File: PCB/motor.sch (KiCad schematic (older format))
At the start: 28 parts, among them J3 70543-0003, U3 TMC2130-TA

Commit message: Finished TMC2130 placement.
Motor sheets is now instanced. That way I simply could use
a KiCad plugin to duplicate the layout in Pcbnew.
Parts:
- TP11: value X_OA1 -> OA1
- TP12: value X_OA2 -> OA2
- TP13: value X_OB2 -> OB2
- TP14: value X_OB1 -> OB1
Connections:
- net labels added: DIAG, DIR, EN, SS, STEP, VDD_PWR
- net labels removed: SS_X, VDD_IN, X_DIAG, X_DIR, X_EN, X_STEP

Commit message: Finished placement. Currently routing last paths.
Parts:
- removed C14, C24: 100nF, Capacitor_SMD:C_0603_1608Metric, symbol Device:C
- removed C16, C17, C18, C19: 1nF, Capacitor_SMD:C_0603_1608Metric, symbol Device:C
- removed R12, R13, R15, R16: 100, Resistor_SMD:R_0603_1608Metric, symbol Device:R
- C58: renamed from C22; value 4.7uF -> 10uF
- renumbered C13 to C54, C15 to C55, C20 to C56, C21 to C57, C23 to C59, C25 to C60, C26 to C61, C27 to C62, J3 to J21, R14 to R32, R17 to R33, R18 to R34, TP11 to TP27, TP12 to TP28, TP13 to TP29, TP14 to TP30, U3 to U7
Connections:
- wire segments 63 -> 43
- no-connect marks 19 -> 18
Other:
- moved on the sheet: R12, R14

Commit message: Added the secnd Z connection.
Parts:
- renumbered C54 to C13, C55 to C14, C56 to C15, C57 to C16, C58 to C17, C59 to C18, C60 to C19, C61 to C20, C62 to C21, J21 to J3, R32 to R12, R33 to R13, R34 to R14, TP27 to TP11, TP28 to TP12, TP29 to TP13, TP30 to TP14, U7 to U3

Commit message: First PCB version that is fully placed and routed.
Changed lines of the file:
@@
 AR Path="/5AFC9D86/5AF8CE9A" Ref="#PWR0105"  Part="1"
 AR Path="/5AFD185C/5AF8CE9A" Ref="#PWR0118"  Part="1"
-F 0 "#PWR0118" H 3550 3300 50  0001 C CNN
+F 0 "#PWR092" H 3550 3300 50  0001 C CNN
 F 1 "GNDA" H 3555 3377 50  0000 C CNN
 F 2 "" H 3550 3550 50  0001 C CNN
@@
 AR Path="/5AFC9D86/5B0399AA" Ref="#PWR0100"  Part="1"
 AR Path="/5AFD185C/5B0399AA" Ref="#PWR0113"  Part="1"
-F 0 "#PWR0113" H 1750 1900 50  0001 C CNN
+F 0 "#PWR087" H 1750 1900 50  0001 C CNN
 F 1 "GNDA" V 1755 2023 50  0000 R CNN
 F 2 "" H 1750 2150 50  0001 C CNN
@@
 AR Path="/5AFC9D86/5AF8CE9D" Ref="R33"  Part="1"
 AR Path="/5AFD185C/5AF8CE9D" Ref="R36"  Part="1"
-F 0 "R36" H 4820 2796 50  0000 L CNN
+F 0 "R30" H 4820 2796 50  0000 L CNN
 F 1 "10k" H 4820 2705 50  0000 L CNN
 F 2 "Resistor_SMD:R_0603_1608Metric" V 4680 2750 50  0001 C CNN
@@
 AR Path="/5AFC9D86/5AF8CE9F" Ref="#PWR0104"  Part="1"
 AR Path="/5AFD185C/5AF8CE9F" Ref="#PWR0117"  Part="1"
-F 0 "#PWR0117" H 2450 3300 50  0001 C CNN
+F 0 "#PWR091" H 2450 3300 50  0001 C CNN
 F 1 "GNDA" H 2455 3377 50  0000 C CNN
 F 2 "" H 2450 3550 50  0001 C CNN
@@
 AR Path="/5AFC9D86/5AF8CEA1" Ref="C55"  Part="1"
 AR Path="/5AFD185C/5AF8CEA1" Ref="C64"  Part="1"
-F 0 "C64" H 3565 1646 50  0000 L CNN
+F 0 "C46" H 3565 1646 50  0000 L CNN
 F 1 "100nF" H 3565 1555 50  0000 L CNN
 F 2 "Capacitor_SMD:C_0603_1608Metric" H 3488 1450 50  0001 C CNN
@@
 AR Path="/5AFC9D86/5AF8CEA3" Ref="C56"  Part="1"
 AR Path="/5AFD185C/5AF8CEA3" Ref="C65"  Part="1"
-F 0 "C65" V 3698 1700 50  0000 C CNN
+F 0 "C47" V 3698 1700 50  0000 C CNN
 F 1 "22nF" V 3789 1700 50  0000 C CNN
 F 2 "Capacitor_SMD:C_0603_1608Metric" H 3988 1550 50  0001 C CNN
@@
 AR Path="/5AFC9D86/5B03C54C" Ref="C54"  Part="1"
 AR Path="/5AFD185C/5B03C54C" Ref="C63"  Part="1"
-F 0 "C63" H 3765 1146 50  0000 L CNN
+F 0 "C45" H 3765 1146 50  0000 L CNN
 F 1 "100nF" H 3765 1055 50  0000 L CNN
 F 2 "Capacitor_SMD:C_0603_1608Metric" H 3688 950 50  0001 C CNN
@@
 AR Path="/5AFC9D86/5B03CBB9" Ref="#PWR096"  Part="1"
 AR Path="/5AFD185C/5B03CBB9" Ref="#PWR0109"  Part="1"
-F 0 "#PWR0109" H 3650 1000 50  0001 C CNN
+F 0 "#PWR083" H 3650 1000 50  0001 C CNN
 F 1 "GNDA" H 3655 1077 50  0000 C CNN
 F 2 "" H 3650 1250 50  0001 C CNN
@@
 AR Path="/5AFC9D86/5B03D7F6" Ref="C57"  Part="1"
 AR Path="/5AFD185C/5B03D7F6" Ref="C66"  Part="1"
-F 0 "C66" H 4385 2054 50  0000 R CNN
+F 0 "C48" H 4385 2054 50  0000 R CNN
 F 1 "470nF" H 4385 2145 50  0000 R CNN
 F 2 "Capacitor_SMD:C_0603_1608Metric" H 4538 1950 50  0001 C CNN
@@
 AR Path="/5AFC9D86/5AF8CEA9" Ref="#PWR098"  Part="1"
 AR Path="/5AFD185C/5AF8CEA9" Ref="#PWR0111"  Part="1"
-F 0 "#PWR0111" H 4500 1700 50  0001 C CNN
+F 0 "#PWR085" H 4500 1700 50  0001 C CNN
 F 1 "GNDA" H 4505 1777 50  0000 C CNN
 F 2 "" H 4500 1950 50  0001 C CNN
@@
 AR Path="/5AFC9D86/5AF8CEAA" Ref="C59"  Part="1"
 AR Path="/5AFD185C/5AF8CEAA" Ref="C68"  Part="1"
-F 0 "C68" H 1365 3146 50  0000 L CNN
+F 0 "C50" H 1365 3146 50  0000 L CNN
 F 1 "100nF" H 1365 3055 50  0000 L CNN
 F 2 "Capacitor_SMD:C_0603_1608Metric" H 1288 2950 50  0001 C CNN
@@
 AR Path="/5AFC9D86/5B03E652" Ref="#PWR0103"  Part="1"
 AR Path="/5AFD185C/5B03E652" Ref="#PWR0116"  Part="1"
-F 0 "#PWR0116" H 1250 3000 50  0001 C CNN
+F 0 "#PWR090" H 1250 3000 50  0001 C CNN
 F 1 "GNDA" H 1255 3077 50  0000 C CNN
 F 2 "" H 1250 3250 50  0001 C CNN
@@
 AR Path="/5AFC9D86/5B043BF7" Ref="#PWR0102"  Part="1"
 AR Path="/5AFD185C/5B043BF7" Ref="#PWR0115"  Part="1"
-F 0 "#PWR0115" H 4150 2200 50  0001 C CNN
+F 0 "#PWR089" H 4150 2200 50  0001 C CNN
 F 1 "GNDA" V 4155 2322 50  0000 R CNN
 F 2 "" H 4150 2450 50  0001 C CNN
@@
 AR Path="/5AFC9D86/5AF8CEAE" Ref="C58"  Part="1"
 AR Path="/5AFD185C/5AF8CEAE" Ref="C67"  Part="1"
-F 0 "C67" V 5600 2350 50  0000 R CNN
+F 0 "C49" V 5600 2350 50  0000 R CNN
 F 1 "10uF" V 5700 2450 50  0000 R CNN
 F 2 "Capacitor_SMD:C_0603_1608Metric" H 5488 2200 50  0001 C CNN
@@
 AR Path="/5AFC9D86/5AF8CEAF" Ref="#PWR0101"  Part="1"
 AR Path="/5AFD185C/5AF8CEAF" Ref="#PWR0114"  Part="1"
-F 0 "#PWR0114" H 5600 2100 50  0001 C CNN
+F 0 "#PWR088" H 5600 2100 50  0001 C CNN
 F 1 "GNDA" H 5605 2177 50  0000 C CNN
 F 2 "" H 5600 2350 50  0001 C CNN
@@
 AR Path="/5AFC9D86/5AF8CEB0" Ref="R34"  Part="1"
 AR Path="/5AFD185C/5AF8CEB0" Ref="R37"  Part="1"
-F 0 "R37" H 3100 4050 50  0000 R CNN
+F 0 "R31" H 3100 4050 50  0000 R CNN
 F 1 "0.12" H 3100 4150 50  0000 R CNN
 F 2 "Resistor_SMD:R_1206_3216Metric" V 2780 4100 50  0001 C CNN
@@
 AR Path="/5AFC9D86/5AF8CEB4" Ref="#PWR0106"  Part="1"
 AR Path="/5AFD185C/5AF8CEB4" Ref="#PWR0119"  Part="1"
-F 0 "#PWR0119" H 2850 4000 50  0001 C CNN
+F 0 "#PWR093" H 2850 4000 50  0001 C CNN
 F 1 "GNDA" H 2855 4077 50  0000 C CNN
 F 2 "" H 2850 4250 50  0001 C CNN
@@
 AR Path="/5AFC9D86/5B09FBAD" Ref="J22"  Part="1"
 AR Path="/5AFD185C/5B09FBAD" Ref="J23"  Part="1"
-F 0 "J23" H 7529 1292 50  0000 L CNN
+F 0 "J21" H 7529 1292 50  0000 L CNN
 F 1 "70543-0003" H 7529 1201 50  0000 L CNN
 F 2 "custom-footprints:70543-0003" H 7450 1300 50  0001 C CNN
@@
 AR Path="/5AFC9D86/5B09FBB4" Ref="TP28"  Part="1"
 AR Path="/5AFD185C/5B09FBB4" Ref="TP32"  Part="1"
-F 0 "TP32" H 7058 1220 50  0000 L CNN
+F 0 "TP24" H 7058 1220 50  0000 L CNN
 F 1 "OA2" H 7058 1129 50  0000 L CNN
 F 2 "TestPoint:TestPoint_Pad_D1.0mm" H 7200 1100 50  0001 C CNN
@@
 AR Path="/5AFC9D86/5AF8CEB7" Ref="TP27"  Part="1"
 AR Path="/5AFD185C/5AF8CEB7" Ref="TP31"  Part="1"
-F 0 "TP31" H 6708 1220 50  0000 L CNN
+F 0 "TP23" H 6708 1220 50  0000 L CNN
 F 1 "OA1" H 6708 1129 50  0000 L CNN
 F 2 "TestPoint:TestPoint_Pad_D1.0mm" H 6850 1100 50  0001 C CNN
@@
 AR Path="/5AFC9D86/5AF8CEB9" Ref="TP29"  Part="1"
 AR Path="/5AFD185C/5AF8CEB9" Ref="TP33"  Part="1"
-F 0 "TP33" H 6908 1720 50  0000 L CNN
+F 0 "TP25" H 6908 1720 50  0000 L CNN
 F 1 "OB2" H 6908 1629 50  0000 L CNN
 F 2 "TestPoint:TestPoint_Pad_D1.0mm" H 7050 1600 50  0001 C CNN
@@
 AR Path="/5AFC9D86/5B09FBC9" Ref="TP30"  Part="1"
 AR Path="/5AFD185C/5B09FBC9" Ref="TP34"  Part="1"
-F 0 "TP34" H 7258 1720 50  0000 L CNN
+F 0 "TP26" H 7258 1720 50  0000 L CNN
 F 1 "OB1" H 7258 1629 50  0000 L CNN
 F 2 "TestPoint:TestPoint_Pad_D1.0mm" H 7400 1600 50  0001 C CNN
@@
 AR Path="/5AFC9D86/5AF8CEBE" Ref="#PWR095"  Part="1"
 AR Path="/5AFD185C/5AF8CEBE" Ref="#PWR0108"  Part="1"
-F 0 "#PWR0108" H 2850 800 50  0001 C CNN
+F 0 "#PWR082" H 2850 800 50  0001 C CNN
 F 1 "GNDA" H 2855 877 50  0000 C CNN
 F 2 "" H 2850 1050 50  0001 C CNN
@@
 AR Path="/5AFC9D86/5AF8CED0" Ref="C61"  Part="1"
 AR Path="/5AFD185C/5AF8CED0" Ref="C70"  Part="1"
-F 0 "C70" H 5315 4196 50  0000 L CNN
+F 0 "C52" H 5315 4196 50  0000 L CNN
 F 1 "100nF" H 5315 4105 50  0000 L CNN
 F 2 "Capacitor_SMD:C_0603_1608Metric" H 5238 4000 50  0001 C CNN
@@
 AR Path="/5AFC9D86/5AF8CED2" Ref="C62"  Part="1"
 AR Path="/5AFD185C/5AF8CED2" Ref="C71"  Part="1"
-F 0 "C71" H 5765 4196 50  0000 L CNN
+F 0 "C53" H 5765 4196 50  0000 L CNN
 F 1 "100nF" H 5765 4105 50  0000 L CNN
 F 2 "Capacitor_SMD:C_0603_1608Metric" H 5688 4000 50  0001 C CNN
@@
 AR Path="/5AFC9D86/5B0D4996" Ref="#PWR0107"  Part="1"
 AR Path="/5AFD185C/5B0D4996" Ref="#PWR0120"  Part="1"
-F 0 "#PWR0120" H 4600 4050 50  0001 C CNN
+F 0 "#PWR094" H 4600 4050 50  0001 C CNN
 F 1 "GNDA" V 4605 4173 50  0000 R CNN
 F 2 "" H 4600 4300 50  0001 C CNN
@@
 AR Path="/5AFC9D86/5B0E8E43" Ref="C60"  Part="1"
 AR Path="/5AFD185C/5B0E8E43" Ref="C69"  Part="1"
-F 0 "C69" H 4868 4196 50  0000 L CNN
+F 0 "C51" H 4868 4196 50  0000 L CNN
 F 1 "100uF" H 4868 4105 50  0000 L CNN
 F 2 "Capacitor_THT:CP_Radial_D6.3mm_P2.50mm" H 4788 4000 50  0001 C CNN
@@
 AR Path="/5AFC9D86/5AF83011" Ref="R32"  Part="1"
 AR Path="/5AFD185C/5AF83011" Ref="R35"  Part="1"
-F 0 "R35" H 2750 1150 50  0000 R CNN
+F 0 "R29" H 2750 1150 50  0000 R CNN
 F 1 "0.12" H 2750 1250 50  0000 R CNN
 F 2 "Resistor_SMD:R_1206_3216Metric" V 2780 1200 50  0001 C CNN
@@
 AR Path="/5AFC9D86/5AF8CE97" Ref="#PWR097"  Part="1"
 AR Path="/5AFD185C/5AF8CE97" Ref="#PWR0110"  Part="1"
-F 0 "#PWR0110" H 2350 1300 50  0001 C CNN
+F 0 "#PWR084" H 2350 1300 50  0001 C CNN
 F 1 "GNDA" H 2355 1377 50  0000 C CNN
 F 2 "" H 2350 1550 50  0001 C CNN
@@
 AR Path="/5AFC9D86/5AF8CE98" Ref="U7"  Part="1"
 AR Path="/5AFD185C/5AF8CE98" Ref="U8"  Part="1"
-F 0 "U8" H 2950 2650 50  0000 L CNN
+F 0 "U6" H 2950 2650 50  0000 L CNN
 F 1 "TMC2130-TA" H 2800 2550 50  0000 L CNN
 F 2 "custom-footprints:TQFP-48-1EP_7x7mm_P0.5mm_EP4.8x4.8mm-Heatsink" H 3000 2600 50  0001 C CNN
@@
 AR Path="/5AFC9D86/5AFD58A6" Ref="#PWR099"  Part="1"
 AR Path="/5AFD185C/5AFD58A6" Ref="#PWR0112"  Part="1"
-F 0 "#PWR0112" H 1750 1800 50  0001 C CNN
+F 0 "#PWR086" H 1750 1800 50  0001 C CNN
 F 1 "GNDA" V 1755 1923 50  0000 R CNN
 F 2 "" H 1750 2050 50  0001 C CNN

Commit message: Reworked some traces for better layout.
This will also come in handy, when we add more external
connections (10 to 20pin external).
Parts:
- C13, C14, C15, C16, C17, C18, C20, C21: symbol Device:C -> remram-rescue:C-Device
- C19: symbol Device:CP -> remram-rescue:CP-Device
- J3: symbol Connector_Generic:Conn_01x04 -> remram-rescue:Conn_01x04-Connector_Generic
- R12, R13, R14: symbol Device:R -> remram-rescue:R-Device
- TP11, TP12, TP13, TP14: symbol Connector_Specialized:Test_Point -> remram-rescue:Test_Point-Connector_Specialized
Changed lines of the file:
@@
 AR Path="/5AFC9D86/5AF8CE9A" Ref="#PWR0105"  Part="1"
 AR Path="/5AFD185C/5AF8CE9A" Ref="#PWR0118"  Part="1"
-F 0 "#PWR092" H 3550 3300 50  0001 C CNN
+F 0 "#PWR0118" H 3550 3300 50  0001 C CNN
 F 1 "GNDA" H 3555 3377 50  0000 C CNN
 F 2 "" H 3550 3550 50  0001 C CNN
@@
 AR Path="/5AFC9D86/5B0399AA" Ref="#PWR0100"  Part="1"
 AR Path="/5AFD185C/5B0399AA" Ref="#PWR0113"  Part="1"
-F 0 "#PWR087" H 1750 1900 50  0001 C CNN
+F 0 "#PWR0113" H 1750 1900 50  0001 C CNN
 F 1 "GNDA" V 1755 2023 50  0000 R CNN
 F 2 "" H 1750 2150 50  0001 C CNN
@@
 $EndComp
 $Comp
-L Device:R R13
+L remram-rescue:R-Device R13
 U 1 1 5AF8CE9D
 P 4750 2750
@@
 AR Path="/5AFC9D86/5AF8CE9F" Ref="#PWR0104"  Part="1"
 AR Path="/5AFD185C/5AF8CE9F" Ref="#PWR0117"  Part="1"
-F 0 "#PWR091" H 2450 3300 50  0001 C CNN
+F 0 "#PWR0117" H 2450 3300 50  0001 C CNN
 F 1 "GNDA" H 2455 3377 50  0000 C CNN
 F 2 "" H 2450 3550 50  0001 C CNN
@@
 $EndComp
 $Comp
-L Device:C C14
+L remram-rescue:C-Device C14
 U 1 1 5AF8CEA1
 P 3450 1600
@@
 $EndComp
 $Comp
-L Device:C C15
+L remram-rescue:C-Device C15
 U 1 1 5AF8CEA3
 P 3950 1700
@@
 	4300 1700 4300 2150
 $Comp
-L Device:C C13
+L remram-rescue:C-Device C13
 U 1 1 5B03C54C
 P 3650 1100
@@
 AR Path="/5AFC9D86/5B03CBB9" Ref="#PWR096"  Part="1"
 AR Path="/5AFD185C/5B03CBB9" Ref="#PWR0109"  Part="1"
-F 0 "#PWR083" H 3650 1000 50  0001 C CNN
+F 0 "#PWR0109" H 3650 1000 50  0001 C CNN
 F 1 "GNDA" H 3655 1077 50  0000 C CNN
 F 2 "" H 3650 1250 50  0001 C CNN
@@
 $EndComp
 $Comp
-L Device:C C16
+L remram-rescue:C-Device C16
 U 1 1 5B03D7F6
 P 4500 2100
@@
 AR Path="/5AFC9D86/5AF8CEA9" Ref="#PWR098"  Part="1"
 AR Path="/5AFD185C/5AF8CEA9" Ref="#PWR0111"  Part="1"
-F 0 "#PWR085" H 4500 1700 50  0001 C CNN
+F 0 "#PWR0111" H 4500 1700 50  0001 C CNN
 F 1 "GNDA" H 4505 1777 50  0000 C CNN
 F 2 "" H 4500 1950 50  0001 C CNN
@@
 $EndComp
 $Comp
-L Device:C C18
+L remram-rescue:C-Device C18
 U 1 1 5AF8CEAA
 P 1250 3100
@@
 AR Path="/5AFC9D86/5B03E652" Ref="#PWR0103"  Part="1"
 AR Path="/5AFD185C/5B03E652" Ref="#PWR0116"  Part="1"
-F 0 "#PWR090" H 1250 3000 50  0001 C CNN
+F 0 "#PWR0116" H 1250 3000 50  0001 C CNN
 F 1 "GNDA" H 1255 3077 50  0000 C CNN
 F 2 "" H 1250 3250 50  0001 C CNN
@@
 AR Path="/5AFC9D86/5B043BF7" Ref="#PWR0102"  Part="1"
 AR Path="/5AFD185C/5B043BF7" Ref="#PWR0115"  Part="1"
-F 0 "#PWR089" H 4150 2200 50  0001 C CNN
+F 0 "#PWR0115" H 4150 2200 50  0001 C CNN
 F 1 "GNDA" V 4155 2322 50  0000 R CNN
 F 2 "" H 4150 2450 50  0001 C CNN
@@
 $EndComp
 $Comp
-L Device:C C17
+L remram-rescue:C-Device C17
 U 1 1 5AF8CEAE
 P 5450 2350
@@
 AR Path="/5AFC9D86/5AF8CEAF" Ref="#PWR0101"  Part="1"
 AR Path="/5AFD185C/5AF8CEAF" Ref="#PWR0114"  Part="1"
-F 0 "#PWR088" H 5600 2100 50  0001 C CNN
+F 0 "#PWR0114" H 5600 2100 50  0001 C CNN
 F 1 "GNDA" H 5605 2177 50  0000 C CNN
 F 2 "" H 5600 2350 50  0001 C CNN
@@
 NoConn ~ 3450 3550
 $Comp
-L Device:R R14
+L remram-rescue:R-Device R14
 U 1 1 5AF8CEB0
 P 2850 4100
@@
 AR Path="/5AFC9D86/5AF8CEB4" Ref="#PWR0106"  Part="1"
 AR Path="/5AFD185C/5AF8CEB4" Ref="#PWR0119"  Part="1"
-F 0 "#PWR093" H 2850 4000 50  0001 C CNN
+F 0 "#PWR0119" H 2850 4000 50  0001 C CNN
 F 1 "GNDA" H 2855 4077 50  0000 C CNN
 F 2 "" H 2850 4250 50  0001 C CNN
@@
 	2850 3950 2850 3550
 $Comp
-L Connector_Generic:Conn_01x04 J3
+L remram-rescue:Conn_01x04-Connector_Generic J3
 U 1 1 5B09FBAD
 P 7450 1300
@@
 $EndComp
 $Comp
-L Connector_Specialized:Test_Point TP12
+L remram-rescue:Test_Point-Connector_Specialized TP12
 U 1 1 5B09FBB4
 P 7000 1100
@@
 $EndComp
 $Comp
-L Connector_Specialized:Test_Point TP11
+L remram-rescue:Test_Point-Connector_Specialized TP11
 U 1 1 5AF8CEB7
 P 6650 1100
@@
 $EndComp
 $Comp
-L Connector_Specialized:Test_Point TP13
+L remram-rescue:Test_Point-Connector_Specialized TP13
 U 1 1 5AF8CEB9
 P 6850 1600
@@
 $EndComp
 $Comp
-L Connector_Specialized:Test_Point TP14
+L remram-rescue:Test_Point-Connector_Specialized TP14
 U 1 1 5B09FBC9
 P 7200 1600
@@
 AR Path="/5AFC9D86/5AF8CEBE" Ref="#PWR095"  Part="1"
 AR Path="/5AFD185C/5AF8CEBE" Ref="#PWR0108"  Part="1"
-F 0 "#PWR082" H 2850 800 50  0001 C CNN
+F 0 "#PWR0108" H 2850 800 50  0001 C CNN
 F 1 "GNDA" H 2855 877 50  0000 C CNN
 F 2 "" H 2850 1050 50  0001 C CNN
@@
 Max RMS 1.64A
 $Comp
-L Device:C C20
+L remram-rescue:C-Device C20
 U 1 1 5AF8CED0
 P 5200 4150
@@
 $EndComp
 $Comp
-L Device:C C21
+L remram-rescue:C-Device C21
 U 1 1 5AF8CED2
 P 5650 4150
@@
 AR Path="/5AFC9D86/5B0D4996" Ref="#PWR0107"  Part="1"
 AR Path="/5AFD185C/5B0D4996" Ref="#PWR0120"  Part="1"
-F 0 "#PWR094" H 4600 4050 50  0001 C CNN
+F 0 "#PWR0120" H 4600 4050 50  0001 C CNN
 F 1 "GNDA" V 4605 4173 50  0000 R CNN
 F 2 "" H 4600 4300 50  0001 C CNN
@@
 VDD_PWR
 $Comp
-L Device:CP C19
+L remram-rescue:CP-Device C19
 U 1 1 5B0E8E43
 P 4750 4150
@@
 Connection ~ 4750 4300
 $Comp
-L Device:R R12
+L remram-rescue:R-Device R12
 U 1 1 5AF83011
 P 2850 1200
@@
 AR Path="/5AFC9D86/5AF8CE97" Ref="#PWR097"  Part="1"
 AR Path="/5AFD185C/5AF8CE97" Ref="#PWR0110"  Part="1"
-F 0 "#PWR084" H 2350 1300 50  0001 C CNN
+F 0 "#PWR0110" H 2350 1300 50  0001 C CNN
 F 1 "GNDA" H 2355 1377 50  0000 C CNN
 F 2 "" H 2350 1550 50  0001 C CNN
@@
 AR Path="/5AFC9D86/5AFD58A6" Ref="#PWR099"  Part="1"
 AR Path="/5AFD185C/5AFD58A6" Ref="#PWR0112"  Part="1"
-F 0 "#PWR086" H 1750 1800 50  0001 C CNN
+F 0 "#PWR0112" H 1750 1800 50  0001 C CNN
 F 1 "GNDA" V 1755 1923 50  0000 R CNN
 F 2 "" H 1750 2050 50  0001 C CNN

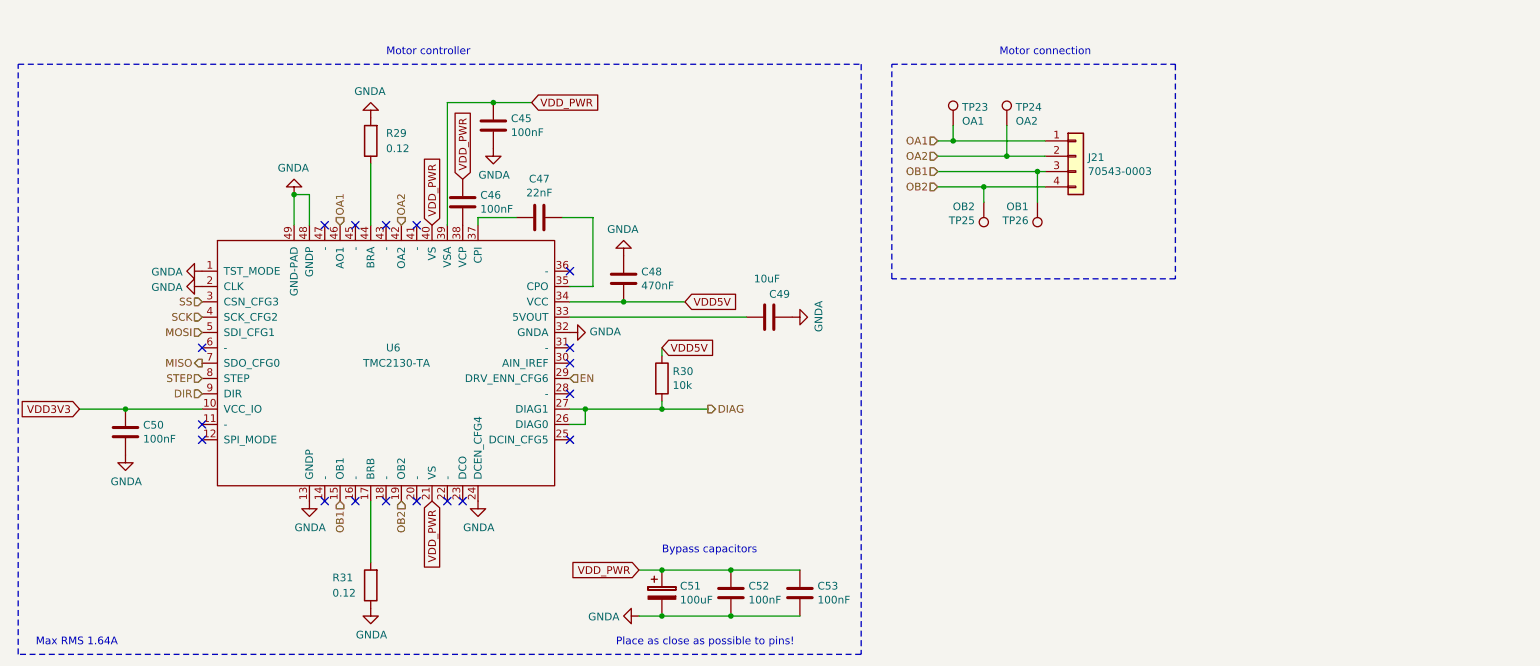
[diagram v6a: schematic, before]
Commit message: Reworked some traces and labels.
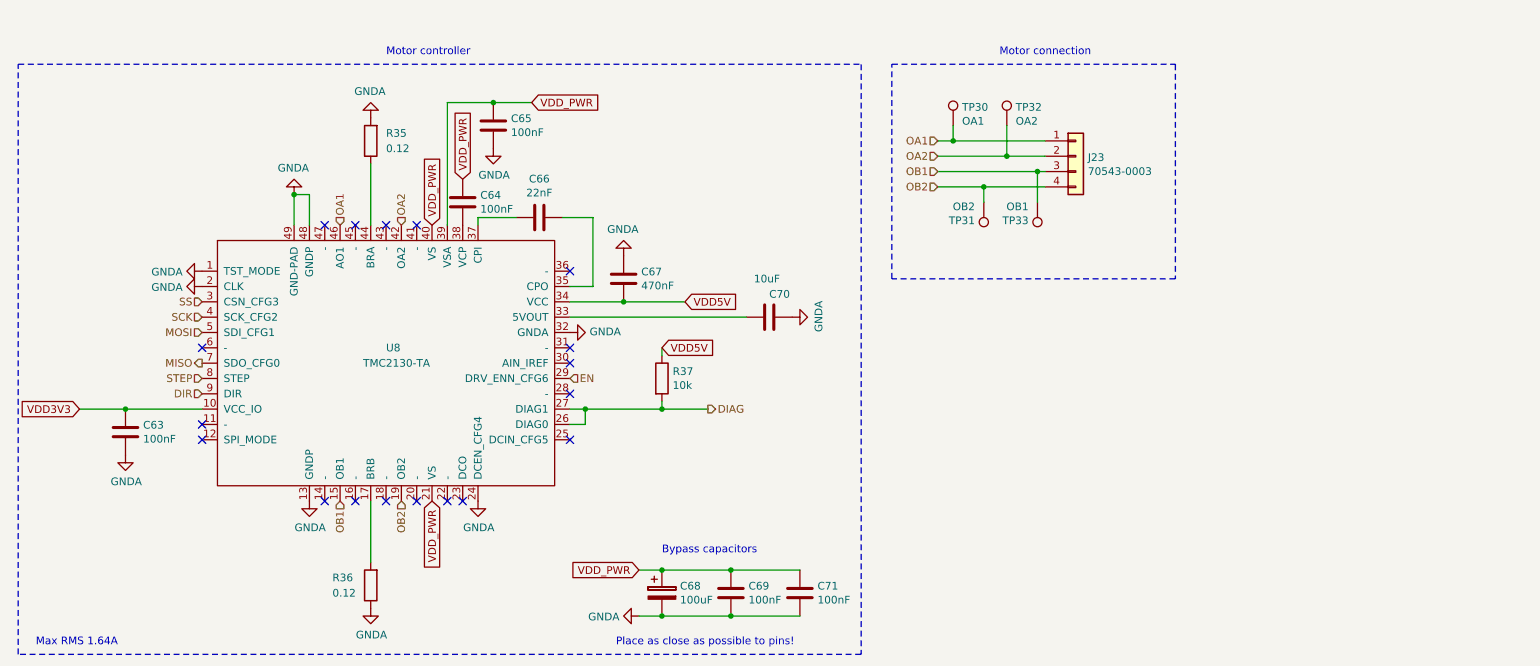
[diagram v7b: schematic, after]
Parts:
- renumbered C18 to C13, C13 to C15, C15 to C16, C16 to C17, C19 to C18, C20 to C19, C17 to C20, R14 to R13, R13 to R14, TP13 to TP12, TP12 to TP13

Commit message: First draft of RemRam.
I added a 20 pin expansion connector with the following pins:
 - SPI
 - I2C
 - USART
 - 4x PWM
 - 4x GPIO
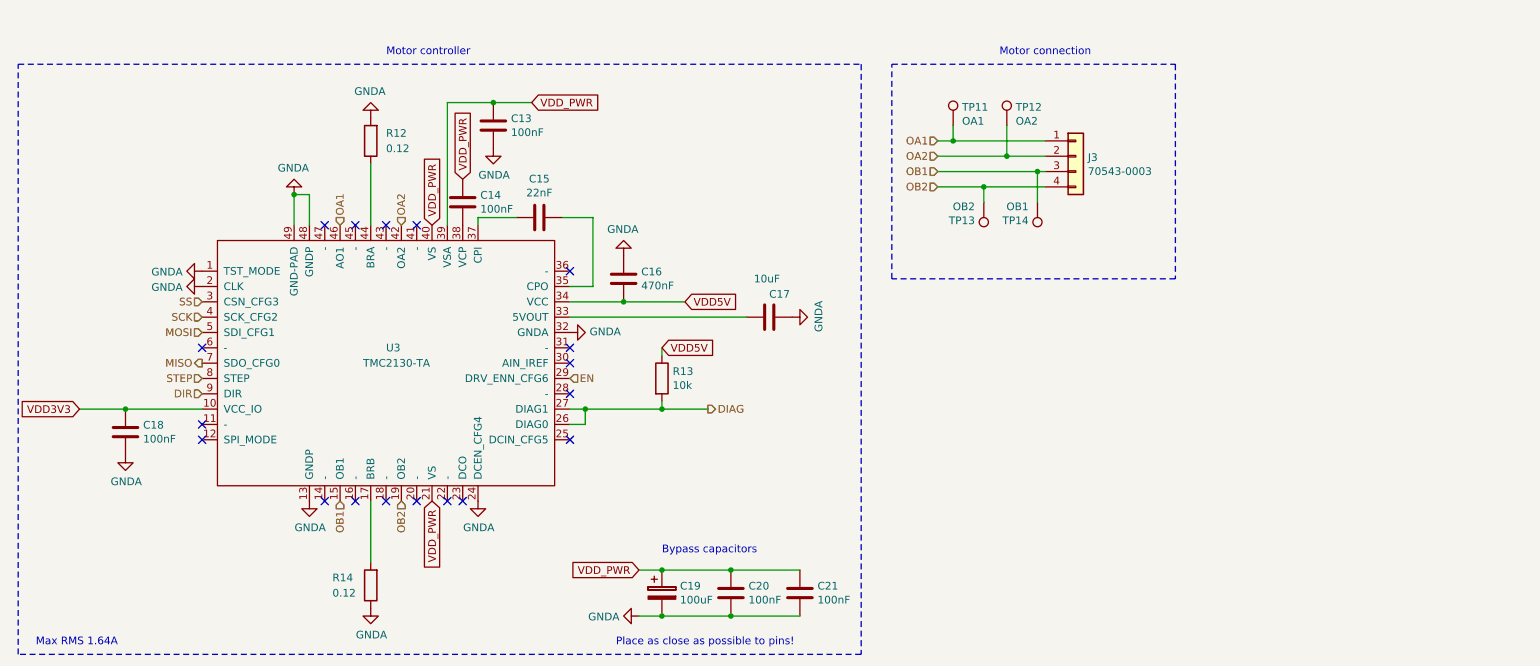
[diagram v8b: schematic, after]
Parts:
- renumbered C15 to C13, C16 to C15, C17 to C16, C20 to C17, C13 to C18, C18 to C19, C19 to C20, R14 to R13, R13 to R14, TP13 to TP12, TP12 to TP13
